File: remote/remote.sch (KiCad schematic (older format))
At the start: 31 parts, among them P1 PAD_R, P2 PAD_L, Q1 Q_PNP_BCE, Q2 Q_PNP_BCE, Q3 Q_NPN_BCE, Q4 Q_NPN_BCE, Q5 Q_PNP_BCE, Q6 Q_PNP_BCE

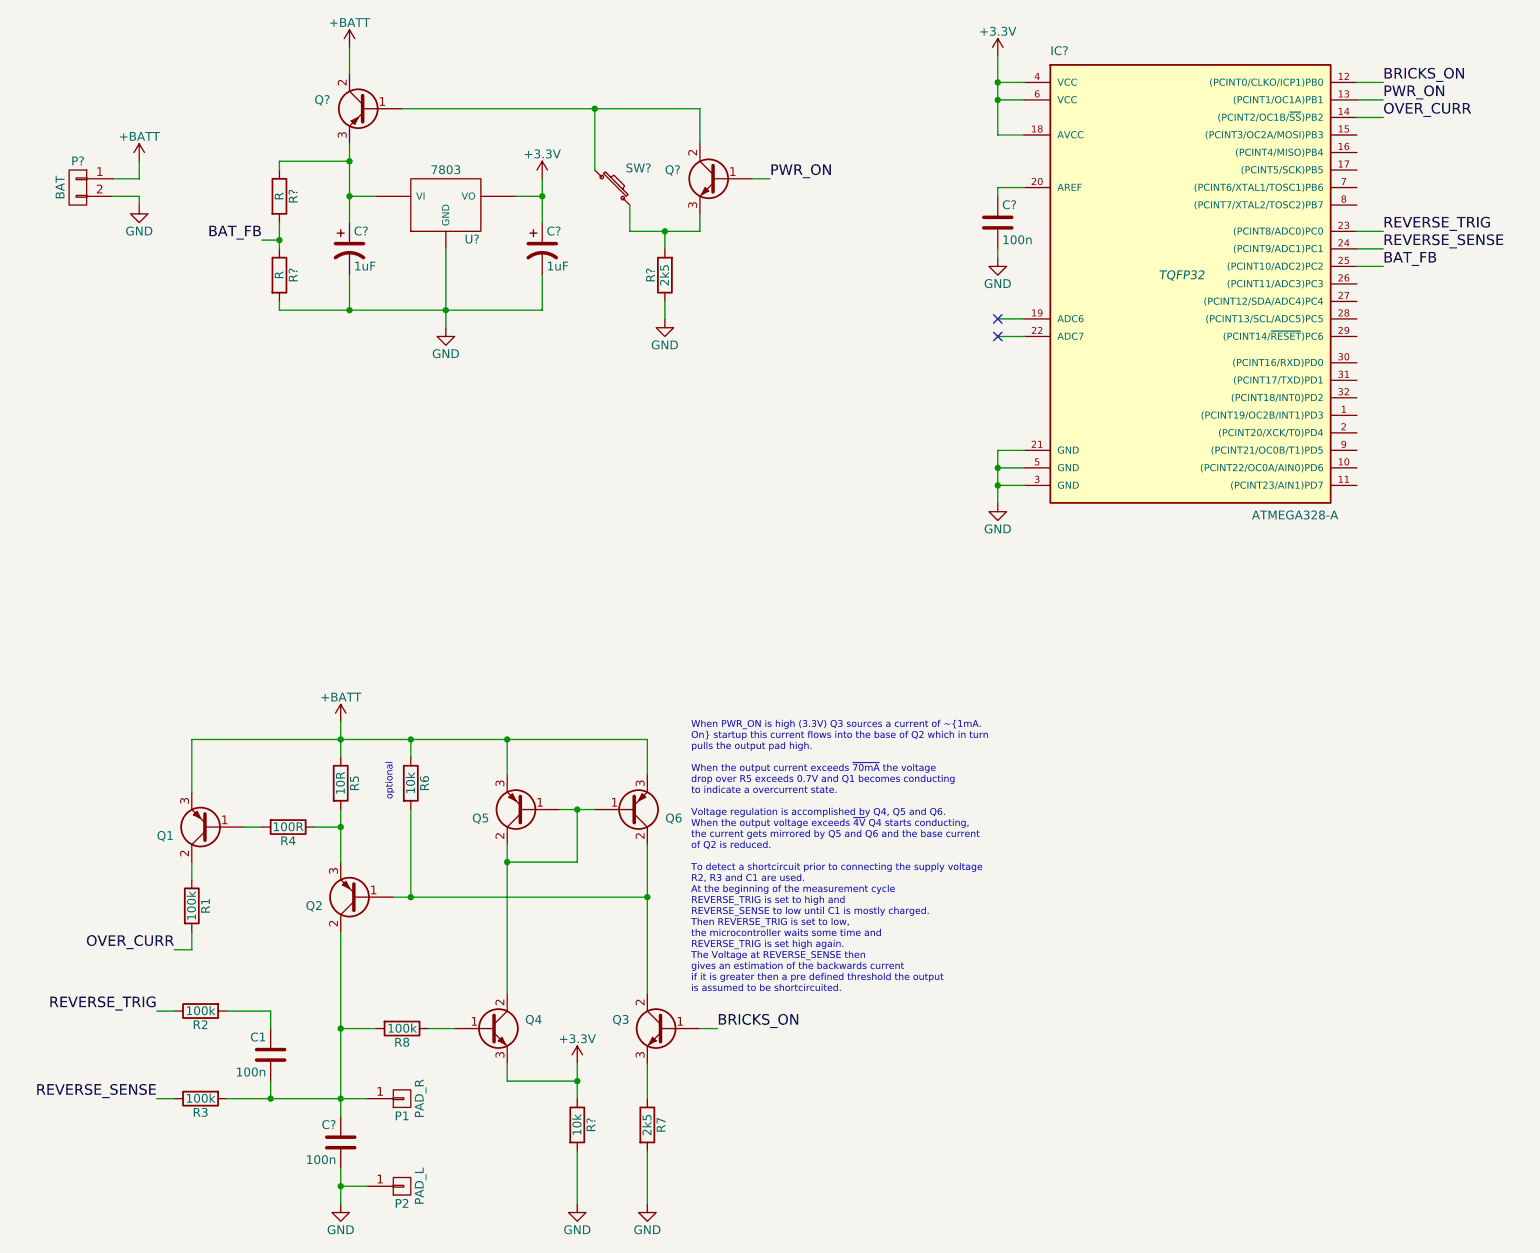
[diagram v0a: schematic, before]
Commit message: rationalized away one transistor
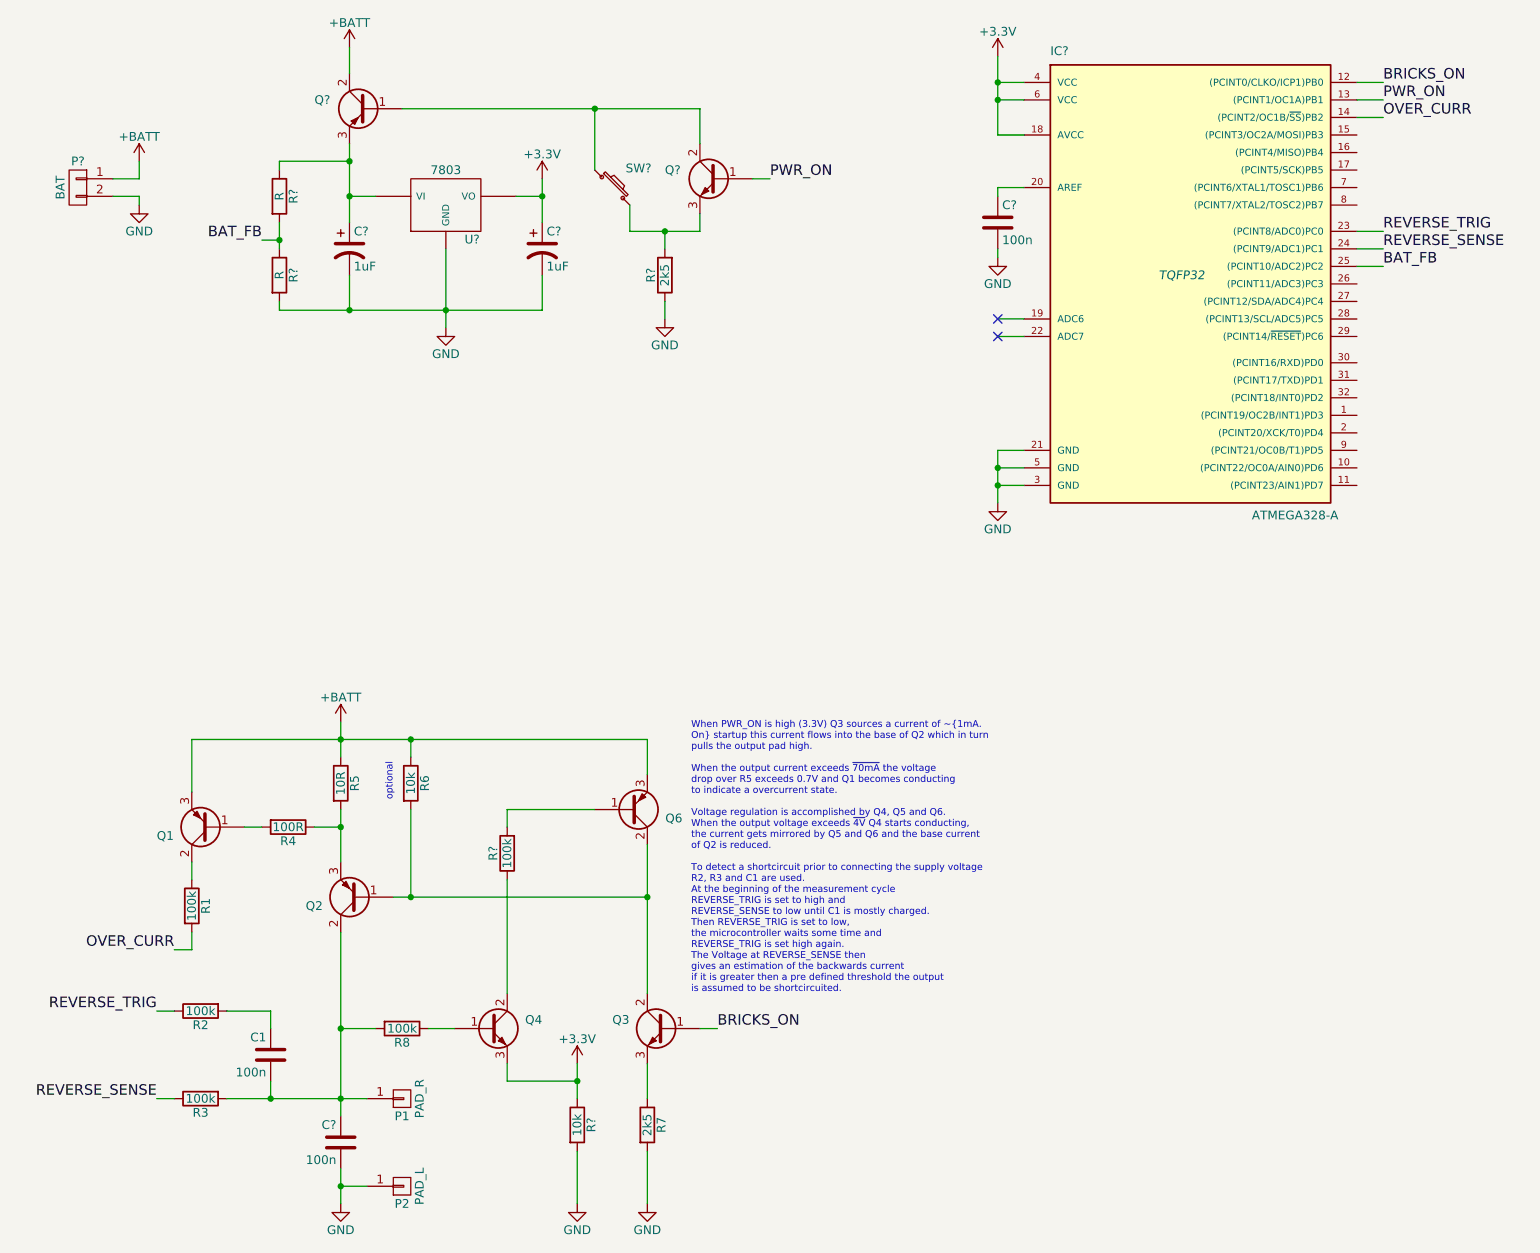
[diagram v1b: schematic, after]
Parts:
- removed Q5: Q_PNP_BCE, symbol Q_PNP_BCE
- added R?: 100k, symbol R
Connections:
- net at Q4.2 (C): now also R?.1; no longer Q6.1 (B)
- new net: Q6.1 (B), R?.2
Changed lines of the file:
@@
 LIBS:contrib
 LIBS:valves
+LIBS:remote-cache
 EELAYER 25 0
 EELAYER END
@@
 $EndComp
 Wire Wire Line
-	2350 5250 2350 5350
-Wire Wire Line
-	2350 5350 2350 5550
-Wire Wire Line
-	2350 4750 2350 4850
-Wire Wire Line
-	2350 4850 2350 4950
+	2350 5250 2350 5550
+Wire Wire Line
+	2350 4750 2350 4950
 $Comp
 L Q_PNP_BCE Q1
@@
 $EndComp
 Wire Wire Line
-	1500 4850 2350 4850
-Wire Wire Line
-	2350 4850 2750 4850
-Wire Wire Line
-	2750 4850 3300 4850
-Wire Wire Line
-	3300 4850 4100 4850
+	1500 4850 4100 4850
 Wire Wire Line
 	1500 4850 1500 5150
@@
 $EndComp
 Wire Wire Line
-	1700 6900 1950 6900
-Wire Wire Line
-	1950 6900 2350 6900
-Wire Wire Line
-	2350 6900 2500 6900
-Wire Wire Line
-	2350 5950 2350 6500
-Wire Wire Line
-	2350 6500 2350 6900
-Wire Wire Line
-	2350 6900 2350 7000
+	1700 6900 2500 6900
+Wire Wire Line
+	2350 5950 2350 7000
 $Comp
 L C C1
@@
 $EndComp
 Wire Wire Line
-	2350 7300 2350 7400
-Wire Wire Line
-	2350 7400 2350 7500
+	2350 7300 2350 7500
 Wire Wire Line
 	2350 7400 2500 7400
@@
 	4100 6900 4100 6700
 Wire Wire Line
-	2650 5750 2750 5750
-Wire Wire Line
-	2750 5750 4100 5750
+	2650 5750 4100 5750
 Text Label 4500 6500 0    60   ~ 0
 BRICKS_ON
@@
 Connection ~ 2350 6500
 $Comp
-L Q_PNP_BCE Q5
-U 1 1 571E01C1
-P 3400 5250
-F 0 "Q5" H 3700 5300 50  0000 R CNN
-F 1 "Q_PNP_BCE" H 4000 5200 50  0001 R CNN
-F 2 "" H 3600 5350 50  0000 C CNN
-F 3 "" H 3400 5250 50  0000 C CNN
-	1    3400 5250
-	-1   0    0    1
-$EndComp
-$Comp
 L Q_PNP_BCE Q6
 U 1 1 571E02BF
@@
 $EndComp
 Wire Wire Line
-	3600 5250 3700 5250
-Wire Wire Line
-	3700 5250 3800 5250
-Wire Wire Line
-	3300 5450 3300 5550
-Wire Wire Line
-	3300 5550 3300 6300
-Wire Wire Line
-	3300 5550 3700 5550
-Wire Wire Line
-	3700 5550 3700 5250
-Connection ~ 3700 5250
-Connection ~ 3300 5550
+	3300 5250 3800 5250
 Wire Wire Line
 	4100 4850 4100 5050
 Connection ~ 2750 4850
 Wire Wire Line
-	3300 5050 3300 4850
-Connection ~ 3300 4850
-Wire Wire Line
-	4100 5450 4100 5750
-Wire Wire Line
-	4100 5750 4100 6300
+	4100 5450 4100 6300
 Connection ~ 4100 5750
 $Comp
@@
 	6250 1100 6100 1100
 Wire Wire Line
-	6100 950  6100 1100
-Wire Wire Line
-	6100 1100 6100 1200
-Wire Wire Line
-	6100 1200 6100 1400
+	6100 950  6100 1400
 Wire Wire Line
 	6100 1200 6250 1200
@@
 $EndComp
 Wire Wire Line
-	6100 3200 6100 3300
-Wire Wire Line
-	6100 3300 6100 3400
-Wire Wire Line
-	6100 3400 6100 3500
+	6100 3200 6100 3500
 Wire Wire Line
 	6100 3200 6250 3200
@@
 	3700 7200 3700 7500
 Wire Wire Line
-	3700 6700 3700 6800
-Wire Wire Line
-	3700 6800 3700 6900
+	3700 6700 3700 6900
 Wire Wire Line
 	3300 6800 3700 6800
@@
 $EndComp
 Wire Wire Line
-	2400 1450 2400 1550
-Wire Wire Line
-	2400 1550 2400 1750
-Wire Wire Line
-	2400 1750 2400 1900
+	2400 1450 2400 1900
 Connection ~ 2400 1750
 Wire Wire Line
 	3350 1750 3500 1750
 Wire Wire Line
-	3500 1650 3500 1750
-Wire Wire Line
-	3500 1750 3500 1900
+	3500 1650 3500 1900
 Wire Wire Line
 	2400 2200 2400 2400
 Wire Wire Line
-	2000 2400 2400 2400
-Wire Wire Line
-	2400 2400 2950 2400
-Wire Wire Line
-	2950 2400 3500 2400
+	2000 2400 3500 2400
 Wire Wire Line
 	3500 2400 3500 2200
@@
 $EndComp
 Wire Wire Line
-	2950 2050 2950 2400
-Wire Wire Line
-	2950 2400 2950 2500
+	2950 2050 2950 2500
 Connection ~ 2950 2400
 $Comp
@@
 $EndComp
 Wire Wire Line
-	2700 1250 3800 1250
-Wire Wire Line
-	3800 1250 4400 1250
+	2700 1250 4400 1250
 $Comp
 L Q_NPN_BCE Q?
@@
 	4000 1800 4000 1950
 Wire Wire Line
-	4000 1950 4200 1950
-Wire Wire Line
-	4200 1950 4400 1950
+	4000 1950 4400 1950
 Wire Wire Line
 	4400 1950 4400 1850
@@
 Connection ~ 2400 1550
 Wire Wire Line
-	2000 1900 2000 2000
-Wire Wire Line
-	2000 2000 2000 2050
+	2000 1900 2000 2050
 Text Label 1900 2000 2    60   ~ 0
 BAT_FB
@@
 	1900 2000 2000 2000
 Connection ~ 2000 2000
+$Comp
+L R R?
+U 1 1 571E512D
+P 3300 5500
+F 0 "R?" V 3380 5500 50  0000 C CNN
+F 1 "100k" V 3300 5500 50  0000 C CNN
+F 2 "" V 3230 5500 50  0000 C CNN
+F 3 "" H 3300 5500 50  0000 C CNN
+	1    3300 5500
+	-1   0    0    1
+$EndComp
+Wire Wire Line
+	3300 5250 3300 5350
+Wire Wire Line
+	3300 5650 3300 6300
 $EndSCHEMATC
